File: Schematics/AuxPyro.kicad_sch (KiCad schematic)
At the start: 6 parts, among them J4 Drouge, Q2 IRLML2502TRPBF

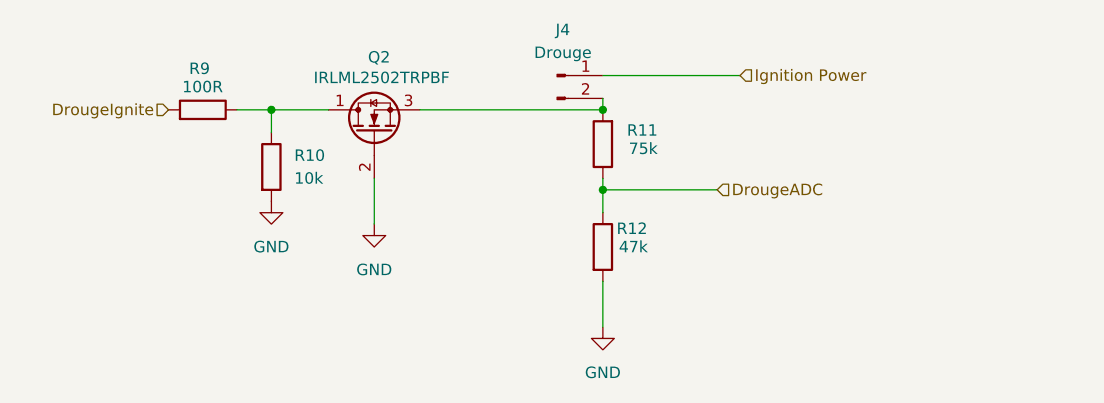
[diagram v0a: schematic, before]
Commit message: added aux pyro added reverse polarity protection re routed just need to clean up and check pin assignments
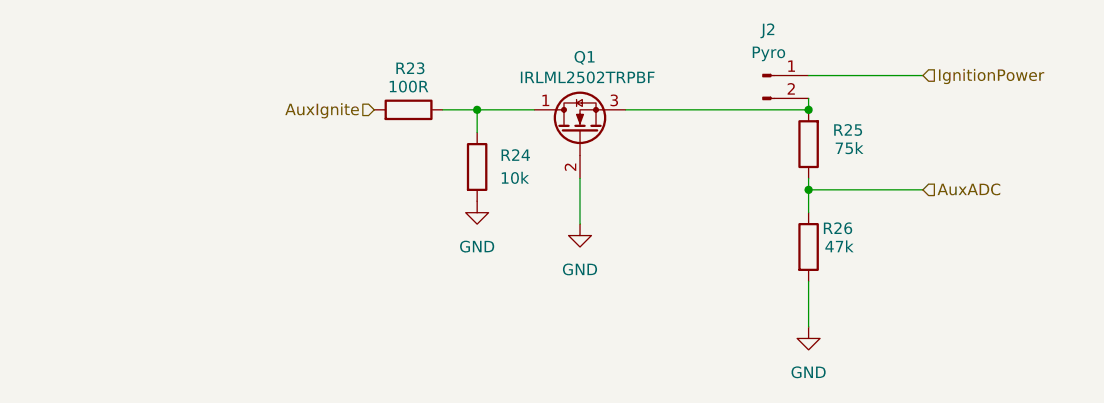
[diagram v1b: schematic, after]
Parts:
- removed J4: Drouge, myFootprints:MOLEX_26013114, symbol Connector:Conn_01x02_Pin
- removed Q2: IRLML2502TRPBF, myFootprints:SOT23, symbol Transistor_FET:Q_NMOS_DGS
- removed R10: 10k, Resistor_SMD:R_0805_2012Metric_Pad1.20x1.40mm_HandSolder, symbol Device:R
- removed R11: 75k, Resistor_SMD:R_0805_2012Metric_Pad1.20x1.40mm_HandSolder, symbol Device:R
- removed R12: 47k, Resistor_SMD:R_0805_2012Metric_Pad1.20x1.40mm_HandSolder, symbol Device:R
- removed R9: 100R, Resistor_SMD:R_0805_2012Metric_Pad1.20x1.40mm_HandSolder, symbol Device:R
- added J2: Pyro, myFootprints:MOLEX_26013114, symbol Connector:Conn_01x02_Pin
- added Q1: IRLML2502TRPBF, myFootprints:SOT23, symbol Transistor_FET:Q_NMOS_DGS
- added R23: 100R, Resistor_SMD:R_0805_2012Metric_Pad1.20x1.40mm_HandSolder, symbol Device:R
- added R24: 10k, Resistor_SMD:R_0805_2012Metric_Pad1.20x1.40mm_HandSolder, symbol Device:R
- added R25: 75k, Resistor_SMD:R_0805_2012Metric_Pad1.20x1.40mm_HandSolder, symbol Device:R
- added R26: 47k, Resistor_SMD:R_0805_2012Metric_Pad1.20x1.40mm_HandSolder, symbol Device:R
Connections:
- net GND: now also Q1.2 (G), R24.2, R26.2
- new net: Q1.1 (D), R23.1, R24.1
- new net: J2.2 (Pin_2), Q1.3 (S), R25.2
- new net AuxADC: R25.1, R26.1
- new net AuxIgnite: R23.2
- new net IgnitionPower: J2.1 (Pin_1)

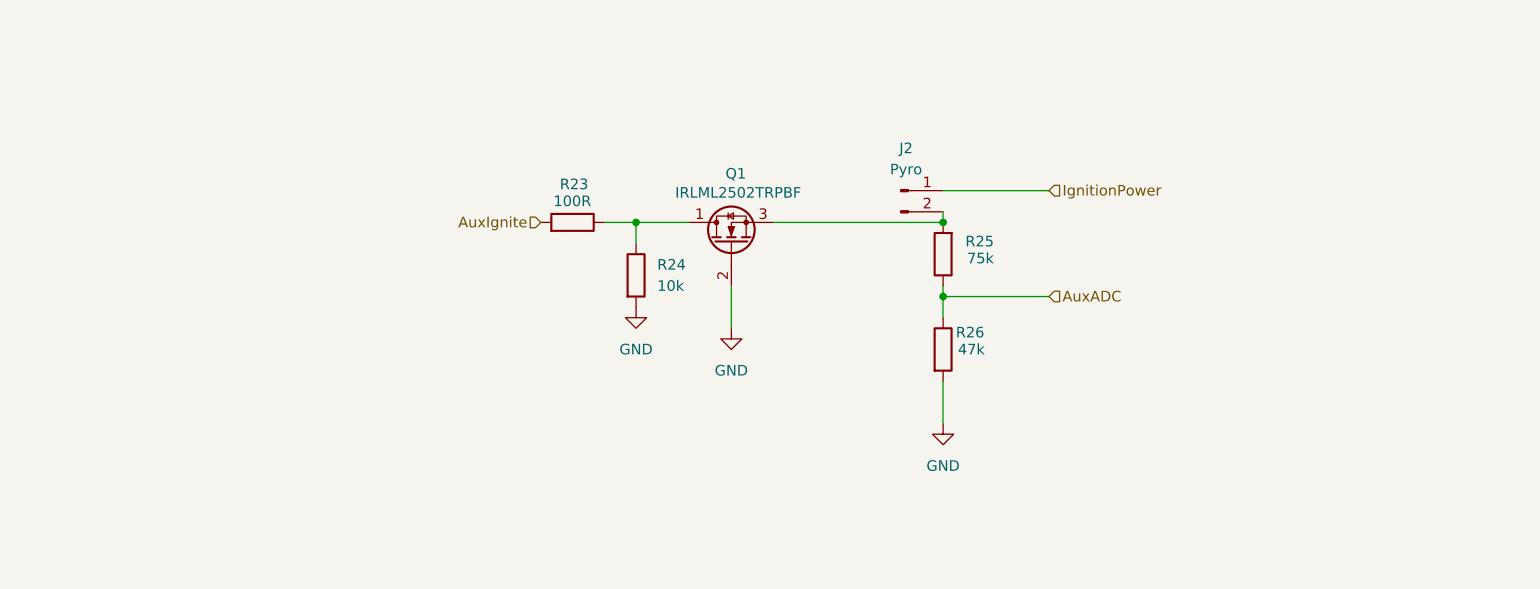
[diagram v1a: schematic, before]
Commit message: layout completed added testpoints and verified mosfet ect
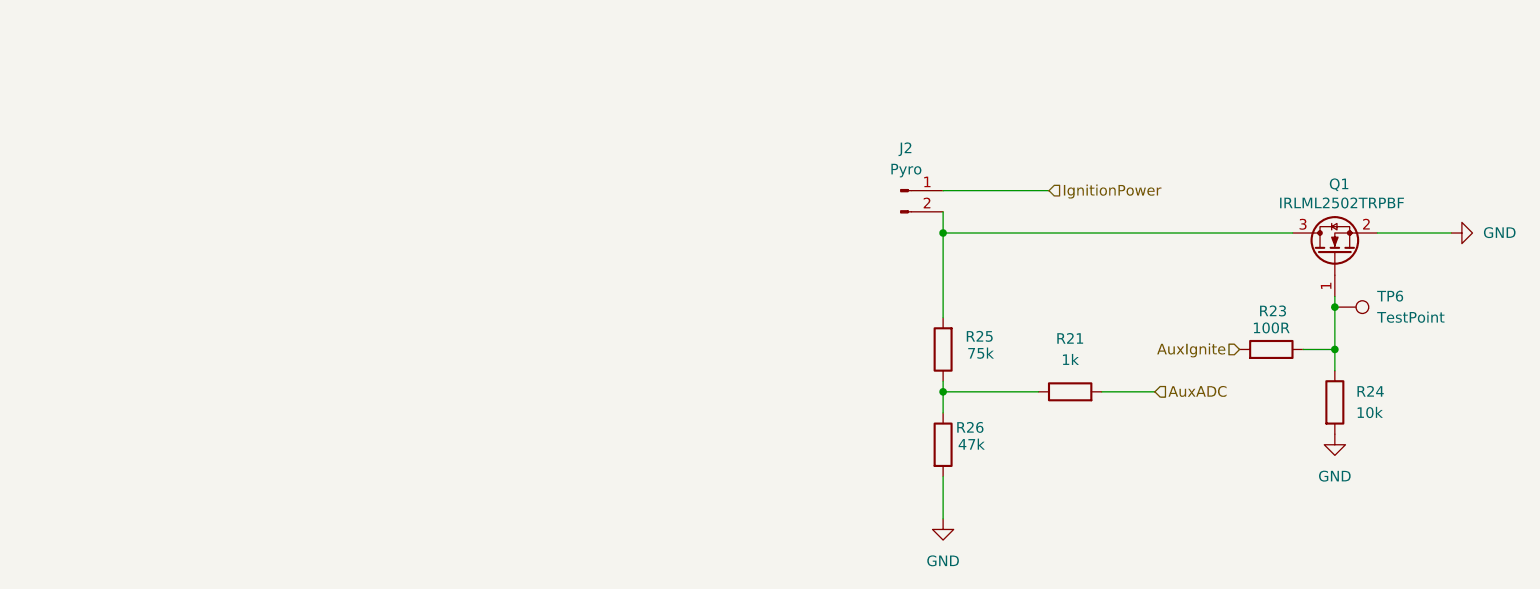
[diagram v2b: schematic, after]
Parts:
- added R21: 1k, Resistor_SMD:R_0805_2012Metric_Pad1.20x1.40mm_HandSolder, symbol Device:R
- added TP6: TestPoint, TestPoint:TestPoint_Pad_1.5x1.5mm, symbol Connector:TestPoint
- Q1: symbol Transistor_FET:Q_NMOS_DGS -> Transistor_FET:Q_NMOS_GSD
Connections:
- net AuxADC: now also R21.2; no longer R25.1, R26.1
- net at Q1.1 (G), R23.1, R24.1: now also TP6.1
- new net: R21.1, R25.1, R26.1
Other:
- moved on the sheet: Q1, R23, R24, R25, R26

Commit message: added comments, awaiting review
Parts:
- R21: LCSC (none) -> C95781
- TP6: now left out of the parts list
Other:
- note added: "Continuity detection with adc resistors to protect adc pins"
- note added: "Low-Side Mosfet Switch for pulling igniton to ground"
- moved on the sheet: J2, Q1, R21, R23, R24, R25, R26, TP6
